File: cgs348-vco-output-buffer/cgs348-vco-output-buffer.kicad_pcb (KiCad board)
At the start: 2 copper layers, 50.3 x 50.8 mm, 27 parts, among them J9 Power, U1 TL074

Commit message: Updating ordered boards
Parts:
- removed H3: Logo_Ammonite-simple, rumblesan-footprints:Logo_Ammonite-simple_10.4mmx12.0mm
- added R10: 47k, rumblesan-footprints:Resistor_THT_L6.3mm_D2.5mm_P10.16mm_Horizontal, F.Cu at (131.3, 124.0)
- added R11: 47k, rumblesan-footprints:Resistor_THT_L6.3mm_D2.5mm_P10.16mm_Horizontal, F.Cu at (97.3, 119.6)
- added R12: 47k, rumblesan-footprints:Resistor_THT_L6.3mm_D2.5mm_P10.16mm_Horizontal, F.Cu at (97.3, 136.1)
- added R13: 47k, rumblesan-footprints:Resistor_THT_L6.3mm_D2.5mm_P10.16mm_Horizontal, F.Cu at (121.2, 133.9)
- added R14: 47k, rumblesan-footprints:Resistor_THT_L6.3mm_D2.5mm_P10.16mm_Horizontal, F.Cu at (121.2, 127.3)
- added R15: 47k, rumblesan-footprints:Resistor_THT_L6.3mm_D2.5mm_P10.16mm_Horizontal, F.Cu at (97.3, 116.3)
- added R16: 47k, rumblesan-footprints:Resistor_THT_L6.3mm_D2.5mm_P10.16mm_Horizontal, F.Cu at (107.4, 132.8)
- added R9: 47k, rumblesan-footprints:Resistor_THT_L6.3mm_D2.5mm_P10.16mm_Horizontal, F.Cu at (131.3, 137.2)
- moved R8 16.3 mm to (99.1, 150.4), turned to 90 degrees
- moved R2 13.9 mm to (131.3, 117.3), turned to 180 degrees
- moved RV4 11.5 mm to (113.8, 135.2)
- moved RV3 10.9 mm to (98.0, 110.5)
- moved RV1 10.8 mm to (125.0, 147.4), turned to 180 degrees
- moved R7 10.8 mm to (97.3, 122.9)
- moved RV2 9.22 mm to (126.5, 111.5)
- moved C2 8.80 mm to (100.2, 104.9), turned to 0 degrees
- moved R6 8.46 mm to (131.3, 120.7)
- moved J7 4.90 mm to (94.0, 122.9)
- moved R5 3.75 mm to (130.8, 141.0), turned to 270 degrees
- moved C1 3.68 mm to (119.4, 104.9)
- moved J3 3.42 mm to (94.0, 119.6)
- moved U1 3.11 mm to (118.1, 129.0)
- moved R4 2.13 mm to (107.4, 129.5)
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- renumbered IN4 to J1, IN3 to J2, IN2 to J3, IN1 to J4, OUT4 to J5, OUT3 to J6, OUT2 to J7, OUT1 to J8
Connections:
- U1 pad 10: Net-(J3-Pad1) -> Net-(R11-Pad2)
- U1 pad 12: Net-(J4-Pad1) -> Net-(R12-Pad2)
- U1 pad 3: Net-(J1-Pad1) -> Net-(R13-Pad1)
- U1 pad 5: Net-(J2-Pad1) -> Net-(R10-Pad2)
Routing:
- net Net-(J1-Pad1): track 20.0 -> 4.56 mm
- net Net-(R5-Pad2): track 15.7 -> 30.9 mm
- net Net-(R11-Pad2): track 0.00 -> 14.9 mm
- net Net-(R13-Pad1): track 0.00 -> 14.5 mm
- net Net-(J2-Pad1): track 17.1 -> 3.30 mm
- net Net-(R12-Pad2): track 0.00 -> 13.5 mm
- net Net-(R3-Pad1): track 11.7 -> 25.0 mm
- net Net-(J4-Pad1): track 17.5 -> 4.25 mm
- net Net-(R1-Pad1): track 10.1 -> 22.7 mm
- net Net-(J3-Pad1): track 15.1 -> 3.30 mm
- net Net-(R7-Pad2): track 15.8 -> 26.9 mm
- net Net-(R10-Pad2): track 0.00 -> 9.64 mm
- net Net-(R6-Pad2): track 15.5 -> 24.1 mm
- net Net-(J6-Pad1): track 9.25 -> 3.30 mm
- net Net-(J7-Pad1): track 7.56 -> 3.30 mm
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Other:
- rule pad_to_mask_clearance: 0.0508 -> 0
- board text added: "CGS348 VCO Output Amp r02"
- board text added: "IN 1"
- board text added: "IN 2"
- board text added: "IN 3"
- board text added: "IN 4"
- board text added: "OUT 4"
- board text added: "OUT1"
- board text added: "OUT2"
- board text added: "OUT3"
- board text removed: "CGS348 VCO Output Amp r01"

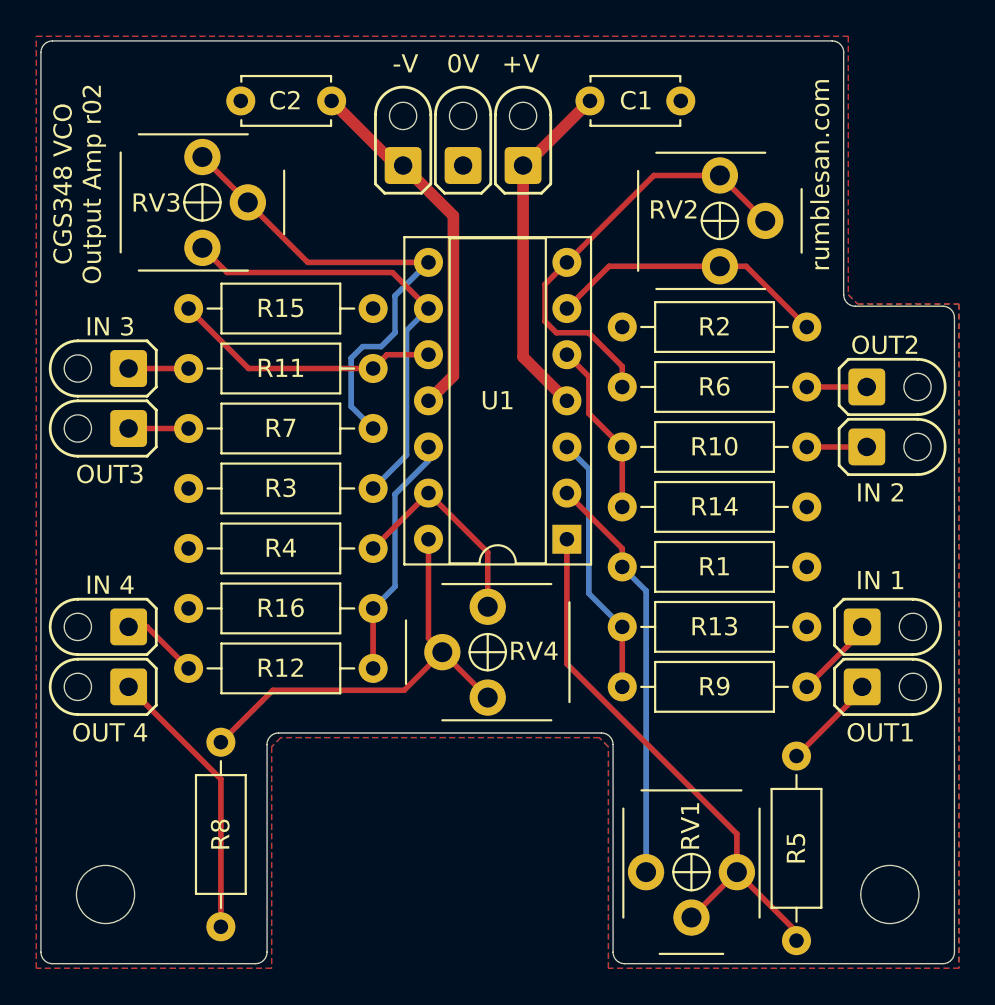
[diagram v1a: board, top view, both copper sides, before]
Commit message: Updating 348 vco output buffer
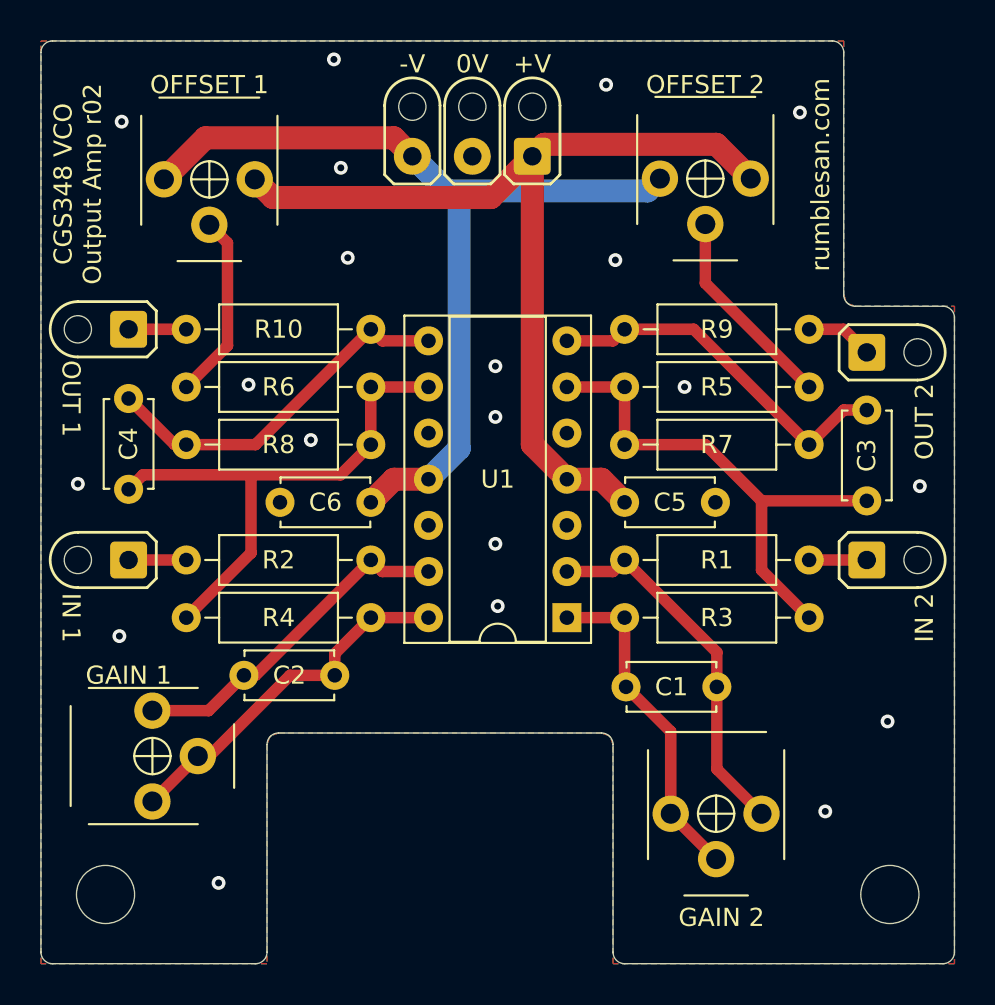
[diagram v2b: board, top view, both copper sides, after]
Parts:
- removed J6, J7, J8: Wire_24AWG_Stranded, rumblesan-footprints:SolderWire-24AWG-0.2sqmm_1x01_D0.5mm_OD1.1mm_Relief
- removed J9: Power, rumblesan-footprints:SolderWire-24AWG-0.2sqmm_1x03_D0.5mm_OD1.1mm_Relief
- removed R11, R12, R13, R14, R15, R16: 47k, rumblesan-footprints:Resistor_THT_L6.3mm_D2.5mm_P10.16mm_Horizontal
- added C3: 5pF, Capacitor_THT:C_Disc_D4.7mm_W2.5mm_P5.00mm, F.Cu at (134.6, 126.9)
- added C4: 5pF, Capacitor_THT:C_Disc_D4.7mm_W2.5mm_P5.00mm, F.Cu at (94.0, 126.3)
- added C5: 100nF, Capacitor_THT:C_Disc_D4.7mm_W2.5mm_P5.00mm, F.Cu at (121.3, 127.0)
- added C6: 100nF, Capacitor_THT:C_Disc_D4.7mm_W2.5mm_P5.00mm, F.Cu at (102.3, 127.0)
- C1, C2: value 100nF -> 5pF
- J1, J2, J3, J4: footprint rumblesan-footprints:SolderWire-24AWG-0.2sqmm_1x01_D0.5mm_OD1.1mm_Relief -> Rumblesan_Footprints:SolderWire-24AWG-0.2sqmm_1x01_D0.5mm_OD1.1mm_Relief
- J5: value Wire_24AWG_Stranded -> Power; footprint rumblesan-footprints:SolderWire-24AWG-0.2sqmm_1x01_D0.5mm_OD1.1mm_Relief -> Rumblesan_Footprints:SolderWire-24AWG-0.2sqmm_1x03_D0.5mm_OD1.1mm_Relief
- R1, R2, R3, R4: footprint rumblesan-footprints:Resistor_THT_L6.3mm_D2.5mm_P10.16mm_Horizontal -> Rumblesan_Footprints:Resistor_THT_L6.3mm_D2.5mm_P10.16mm_Horizontal
- R10, R9: value 47k -> 330; footprint rumblesan-footprints:Resistor_THT_L6.3mm_D2.5mm_P10.16mm_Horizontal -> Rumblesan_Footprints:Resistor_THT_L6.3mm_D2.5mm_P10.16mm_Horizontal
- R5, R6, R7: value 1k -> 4k7; footprint rumblesan-footprints:Resistor_THT_L6.3mm_D2.5mm_P10.16mm_Horizontal -> Rumblesan_Footprints:Resistor_THT_L6.3mm_D2.5mm_P10.16mm_Horizontal
- R8: value 1k -> 47k; footprint rumblesan-footprints:Resistor_THT_L6.3mm_D2.5mm_P10.16mm_Horizontal -> Rumblesan_Footprints:Resistor_THT_L6.3mm_D2.5mm_P10.16mm_Horizontal
- RV1, RV2, RV3, RV4: footprint rumblesan-footprints:Potentiometer_THT_Bourns_3306P_Vertical -> Rumblesan_Footprints:Potentiometer_THT_Bourns_3306P_Vertical
- moved RV2 42.9 mm to (95.3, 141.0)
- moved J2 41.1 mm to (94.0, 130.2), turned to -90 degrees
- moved J3 40.6 mm to (134.6, 118.7), turned to 90 degrees
- moved R2 36.5 mm to (97.2, 130.2), turned to 0 degrees
- moved R10 34.8 mm to (97.2, 117.5), turned to 0 degrees
- moved J5 34.4 mm to (116.2, 108.0), turned to 180 degrees
- moved R7 34.2 mm to (131.4, 123.8), turned to 180 degrees
- moved R6 34.2 mm to (97.2, 120.7), turned to 0 degrees
- moved C1 33.0 mm to (126.4, 137.2), turned to 180 degrees
- moved C2 31.6 mm to (100.3, 136.5)
- moved RV4 30.2 mm to (98.4, 109.2), turned to 180 degrees
- moved RV3 27.7 mm to (125.7, 109.2), turned to 180 degrees
- moved R8 26.6 mm to (97.2, 123.8), turned to 0 degrees
- moved R3 25.0 mm to (131.4, 133.3)
- moved R5 20.3 mm to (131.4, 120.7), turned to 180 degrees
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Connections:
- C1 pad 1: +12V -> Net-(C1-Pad1)
- C1 pad 2: GND -> Net-(C1-Pad2)
- C2 pad 1: GND -> Net-(C2-Pad1)
- C2 pad 2: -12V -> Net-(C2-Pad2)
- J5 pad 1: Net-(J5-Pad1) -> +12V
- R1 pad 1: Net-(R1-Pad1) -> Net-(J1-Pad1)
- R1 pad 2: GND -> Net-(C1-Pad1)
- R10 pad 1: Net-(J2-Pad1) -> Net-(J4-Pad1)
- R10 pad 2: Net-(R10-Pad2) -> Net-(C4-Pad2)
- R2 pad 1: Net-(R2-Pad1) -> Net-(J2-Pad1)
- R2 pad 2: GND -> Net-(C2-Pad1)
- R3 pad 1: Net-(R3-Pad1) -> Net-(C3-Pad1)
- R3 pad 2: GND -> Net-(C1-Pad2)
- R4 pad 1: Net-(R4-Pad1) -> Net-(C4-Pad1)
- R4 pad 2: GND -> Net-(C2-Pad2)
- R5 pad 1: Net-(J5-Pad1) -> Net-(R5-Pad1)
- R5 pad 2: Net-(R5-Pad2) -> Net-(C3-Pad1)
- R6 pad 1: Net-(J6-Pad1) -> Net-(R6-Pad1)
- R6 pad 2: Net-(R6-Pad2) -> Net-(C4-Pad1)
- R7 pad 1: Net-(J7-Pad1) -> Net-(C3-Pad2)
- R7 pad 2: Net-(R7-Pad2) -> Net-(C3-Pad1)
- R8 pad 1: Net-(J8-Pad1) -> Net-(C4-Pad2)
- R8 pad 2: Net-(R8-Pad2) -> Net-(C4-Pad1)
- R9 pad 1: Net-(J1-Pad1) -> Net-(J3-Pad1)
- R9 pad 2: Net-(R13-Pad1) -> Net-(C3-Pad2)
- RV1 pad 1: Net-(R5-Pad2) -> Net-(C1-Pad1)
- RV1 pad 2: Net-(R5-Pad2) -> Net-(C1-Pad2)
- RV1 pad 3: Net-(R1-Pad1) -> Net-(C1-Pad2)
- RV2 pad 1: Net-(R6-Pad2) -> Net-(C2-Pad1)
- RV2 pad 2: Net-(R6-Pad2) -> Net-(C2-Pad2)
- RV2 pad 3: Net-(R2-Pad1) -> Net-(C2-Pad2)
- RV3 pad 1: Net-(R7-Pad2) -> +12V
- RV3 pad 2: Net-(R7-Pad2) -> Net-(R5-Pad1)
- RV3 pad 3: Net-(R3-Pad1) -> -12V
- RV4 pad 1: Net-(R8-Pad2) -> +12V
- RV4 pad 2: Net-(R8-Pad2) -> Net-(R6-Pad1)
- RV4 pad 3: Net-(R4-Pad1) -> -12V
- U1 pad 1: Net-(R5-Pad2) -> Net-(C1-Pad2)
- U1 pad 10: Net-(R11-Pad2) -> GND
- U1 pad 12: Net-(R12-Pad2) -> GND
- U1 pad 13: Net-(R4-Pad1) -> Net-(C2-Pad1)
- U1 pad 14: Net-(R8-Pad2) -> Net-(C2-Pad2)
- U1 pad 2: Net-(R1-Pad1) -> Net-(C1-Pad1)
- U1 pad 3: Net-(R13-Pad1) -> GND
- U1 pad 5: Net-(R10-Pad2) -> GND
- U1 pad 6: Net-(R2-Pad1) -> Net-(C3-Pad1)
- U1 pad 7: Net-(R6-Pad2) -> Net-(C3-Pad2)
- U1 pad 8: Net-(R7-Pad2) -> Net-(C4-Pad2)
- U1 pad 9: Net-(R3-Pad1) -> Net-(C4-Pad1)
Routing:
- net -12V: track 20.1 -> 53.0 mm
- net +12V: track 19.1 -> 52.0 mm
- net Net-(R5-Pad2): track 30.9 -> 0.00 mm
- net Net-(C4-Pad1): track 0.00 -> 30.0 mm
- net Net-(C3-Pad1): track 0.00 -> 28.5 mm
- net Net-(R7-Pad2): track 26.9 -> 0.00 mm
- net Net-(R3-Pad1): track 25.0 -> 0.00 mm
- net Net-(R8-Pad2): track 24.3 -> 0.00 mm
- net Net-(R6-Pad2): track 24.1 -> 0.00 mm
- net Net-(R1-Pad1): track 22.7 -> 0.00 mm
- net Net-(C1-Pad1): track 0.00 -> 20.5 mm
- net Net-(C4-Pad2): track 0.00 -> 20.5 mm
- net Net-(C3-Pad2): track 0.00 -> 20.2 mm
- net Net-(C2-Pad2): track 0.00 -> 20.1 mm
- net Net-(C2-Pad1): track 0.00 -> 18.9 mm
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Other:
- net class Default removed
- net class Power removed
- net class Signal removed
- board text added: "GAIN 1"
- board text added: "GAIN 2"
- board text added: "OFFSET 1"
- board text added: "OFFSET 2"
- board text added: "OUT 1"
- board text added: "OUT 2"
- board text removed: "IN 3"
- board text removed: "IN 4"
- board text removed: "OUT 4"
- board text removed: "OUT1"
- board text removed: "OUT2"
- board text removed: "OUT3"
